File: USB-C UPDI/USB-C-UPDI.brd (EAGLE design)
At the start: 27.4 x 18.3 mm, 9 parts, among them IC1 FT232RL, J2 61300511121

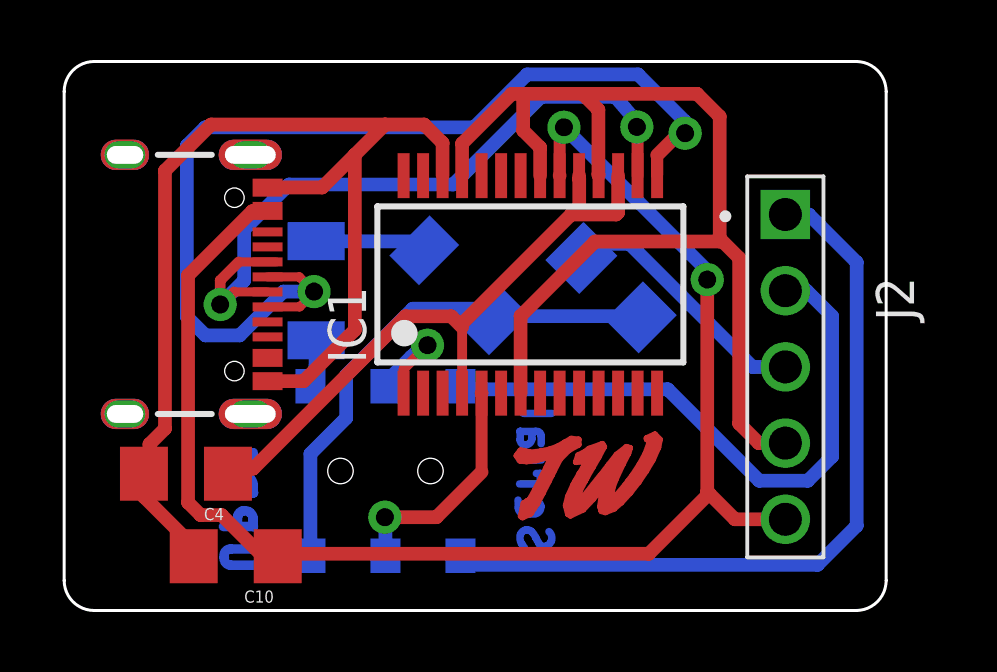
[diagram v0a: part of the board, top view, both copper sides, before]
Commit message: ftid2updi
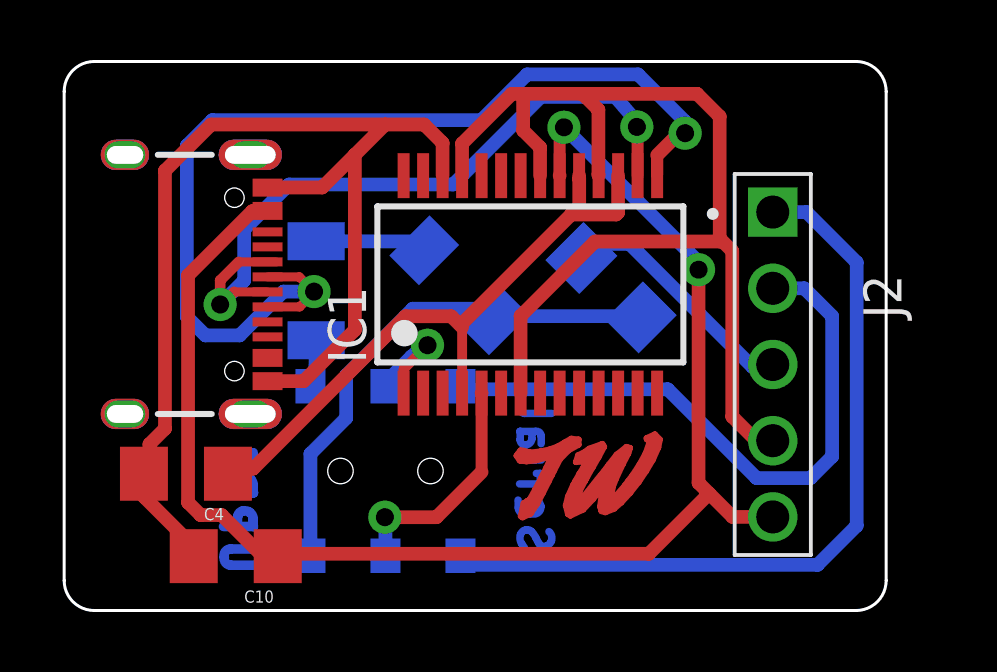
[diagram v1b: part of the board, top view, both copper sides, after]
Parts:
- moved J2 0.43 mm to (23.5, 11.8)

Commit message: updates
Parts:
- moved R1 2.52 mm to (10.8, 14.6), turned to 225 degrees
- moved D1 2.09 mm to (15.2, 14.4)
- moved R2 0.88 mm to (19.0, 14.6), turned to 225 degrees
- moved J2 0.71 mm to (24.2, 11.7)
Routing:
- net N$5: track 29.5 -> 0.00 mm, vias 1 -> 0
- net N$3: track 17.8 -> 3.35 mm
- net N$6: track 1.40 -> 11.5 mm, vias 0 -> 1
- net GND: track 78.1 -> 87.6 mm
- net VCC: track 48.4 -> 57.3 mm
- net N$10: track 4.02 -> 12.5 mm
- net N$7: track 7.77 -> 15.4 mm
- net N$11: track 1.58 -> 4.99 mm
- net UPDI: track 8.31 -> 5.05 mm
- net N$2: track 6.29 -> 8.72 mm
- net N$13: track 17.1 -> 16.3 mm
- net N$4: track 3.95 -> 4.61 mm

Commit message: updates
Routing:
- net GND: track 87.6 -> 84.3 mm
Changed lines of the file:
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@@
 <contactref element="J1" pad="VBUS2"/>
 <contactref element="J2" pad="5"/>
-<wire x1="16.4592" y1="20.1372" x2="16.3992" y2="20.1372" width="0.4572" layer="16"/>
+<wire x1="16.4592" y1="20.1272" x2="16.3992" y2="20.1272" width="0.4572" layer="16"/>
 <wire x1="21.746" y1="15.0004" x2="21.596" y2="15.0004" width="0.4572" layer="16"/>
-<via x="16.3992" y="20.1372" extent="1-16" drill="0.85" diameter="1.8"/>
+<via x="16.3992" y="20.1272" extent="1-16" drill="0.85" diameter="1.7"/>
 <via x="21.746" y="15.0004" extent="1-16" drill="0.85" diameter="1.8"/>
-<wire x1="16.3992" y1="20.1372" x2="16.417175" y2="20.119225" width="0.4572" layer="1"/>
-<wire x1="16.417175" y1="20.119225" x2="16.417175" y2="18.097175" width="0.4572" layer="1"/>
+<wire x1="16.3992" y1="20.1272" x2="16.417175" y2="20.109225" width="0.4572" layer="1"/>
+<wire x1="16.417175" y1="20.109225" x2="16.417175" y2="18.097175" width="0.4572" layer="1"/>
 <wire x1="16.417175" y1="18.097175" x2="16.415" y2="18.095" width="0.4572" layer="1"/>
 <wire x1="24.23" y1="6.66" x2="22.24" y2="6.66" width="0.4572" layer="1"/>
@@
 <wire x1="4.45" y1="6.78" x2="5.15" y2="6.78" width="0.4572" layer="1"/>
 <wire x1="17.031" y1="21.441" x2="20.42" y2="21.441" width="0.4572" layer="16"/>
-<wire x1="16.3992" y1="20.1372" x2="16.3992" y2="20.8092" width="0.4572" layer="16"/>
+<wire x1="16.3992" y1="20.1272" x2="16.3992" y2="20.8092" width="0.4572" layer="16"/>
 <wire x1="17.031" y1="21.441" x2="16.3992" y2="20.8092" width="0.4572" layer="16"/>
 <wire x1="20.42" y1="21.441" x2="22.74" y2="19.121" width="0.4572" layer="16"/>
 <wire x1="22.74" y1="16.07" x2="21.66" y2="14.99" width="0.4572" layer="16"/>
 <wire x1="22.74" y1="19.121" x2="22.74" y2="16.07" width="0.4572" layer="16"/>
-<wire x1="21.746" y1="15.0004" x2="21.66" y2="14.99" width="0" layer="19" extent="16-16"/>
+<wire x1="21.596" y1="15.0004" x2="21.66" y2="14.99" width="0" layer="19" extent="16-16"/>
 <wire x1="21.79" y1="7.07" x2="24.23" y2="6.66" width="0" layer="19" extent="1-1"/>
 <wire x1="6.68" y1="12.02" x2="6.68" y2="16.92" width="0" layer="19" extent="1-1"/>
@@
 <wire x1="12.515" y1="18.095" x2="12.515" y2="19.8" width="0.4572" layer="1"/>
 <wire x1="2.7432" y1="9.144" x2="3.23" y2="9.6308" width="0.4572" layer="1"/>
-<wire x1="4.8" y1="19.8" x2="9.14" y2="19.8" width="0.4572" layer="1"/>
+<wire x1="4.8" y1="19.8" x2="10.49" y2="19.8" width="0.4572" layer="1"/>
 <wire x1="10.49" y1="19.8" x2="12.515" y2="19.8" width="0.4572" layer="1"/>
-<wire x1="6.68" y1="17.695" x2="6.685" y2="17.7" width="0.4572" layer="1"/>
-<wire x1="7.04" y1="17.7" x2="9.14" y2="19.8" width="0.4572" layer="1"/>
+<wire x1="6.725" y1="17.7" x2="6.72" y2="17.695" width="0.4572" layer="1"/>
+<wire x1="6.68" y1="17.695" x2="6.72" y2="17.695" width="0.4572" layer="1"/>
 <wire x1="6.68" y1="11.245" x2="7.885" y2="11.245" width="0.4572" layer="1"/>
 <wire x1="7.885" y1="11.245" x2="10.49" y2="13.85" width="0.4572" layer="1"/>
@@
 <wire x1="13.155" y1="19.715" x2="14.86" y2="21.42" width="0.4572" layer="1"/>
 <wire x1="14.8816" y1="21.4416" x2="15.2" y2="21.4416" width="0.4572" layer="1"/>
-<wire x1="15.765" y1="18.095" x2="15.765" y2="18.935" width="0.4572" layer="1"/>
-<wire x1="15.765" y1="18.935" x2="14.86" y2="19.84" width="0.4572" layer="1"/>
-<wire x1="14.86" y1="19.84" x2="14.86" y2="21.42" width="0.4572" layer="1"/>
+<wire x1="15.765" y1="18.095" x2="15.765" y2="18.905" width="0.4572" layer="1"/>
+<wire x1="15.765" y1="18.905" x2="14.86" y2="19.81" width="0.4572" layer="1"/>
+<wire x1="14.86" y1="19.81" x2="14.86" y2="21.42" width="0.4572" layer="1"/>
 <wire x1="15.2" y1="21.4416" x2="15.2" y2="21.4516" width="0.4572" layer="1"/>
 <wire x1="2.56" y1="8.16" x2="2.56" y2="7.39" width="0.4572" layer="1"/>
@@
 <wire x1="15.115" y1="13.075" x2="16.66" y2="14.62" width="0.4572" layer="1"/>
 <wire x1="16.66" y1="14.62" x2="18.57" y2="14.62" width="0.4572" layer="1"/>
-<wire x1="6.685" y1="17.7" x2="7.04" y2="17.7" width="0.4572" layer="1"/>
-<wire x1="9.14" y1="19.8" x2="10.49" y2="19.8" width="0.4572" layer="1"/>
 <wire x1="10.49" y1="19.8" x2="10.49" y2="13.85" width="0.4572" layer="1"/>
 <wire x1="24.23" y1="9.2" x2="26.13" y2="11.1" width="0.4572" layer="1"/>
@@
 <wire x1="13.07" y1="19.8" x2="13.155" y2="19.715" width="0.4572" layer="1"/>
 <wire x1="15.765" y1="18.095" x2="17.715" y2="18.095" width="0" layer="19" extent="1-1"/>
+<wire x1="6.725" y1="17.7" x2="12.515" y2="18.095" width="0" layer="19" extent="1-1"/>
 </signal>
 <signal name="N$3">
@@
 <contactref element="S1" pad="1"/>
 <wire x1="20.0216" y1="10.9728" x2="13.4112" y2="10.9728" width="0.4572" layer="16"/>
-<wire x1="22.9796" y1="8.0148" x2="20.0216" y2="10.9728" width="0.4572" layer="16"/>
-<wire x1="24.7788" y1="8.0148" x2="22.9796" y2="8.0148" width="0.4572" layer="16"/>
-<wire x1="25.8584" y1="9.0944" x2="24.7788" y2="8.0148" width="0.4572" layer="16"/>
-<wire x1="25.8584" y1="13.0516" x2="25.8584" y2="9.0944" width="0.4572" layer="16"/>
+<wire x1="23.0696" y1="7.9248" x2="20.0216" y2="10.9728" width="0.4572" layer="16"/>
+<wire x1="25.0688" y1="7.9248" x2="23.0696" y2="7.9248" width="0.4572" layer="16"/>
+<wire x1="25.8584" y1="8.7144" x2="25.0688" y2="7.9248" width="0.4572" layer="16"/>
+<wire x1="25.8584" y1="13.0516" x2="25.8584" y2="8.7144" width="0.4572" layer="16"/>
 <wire x1="25.8584" y1="13.0516" x2="24.63" y2="14.28" width="0.4572" layer="16"/>
 <wire x1="24.23" y1="14.28" x2="24.63" y2="14.28" width="0.4572" layer="16"/>

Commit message: updates
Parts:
- added C1: 100nf, 01_SparkFun:1206
- added R3, R4: 5.1k, 01_SparkFun:1206
- added R5, R6: 330, 01_SparkFun:1206
- added RX-LED, TX-LED: LED, eagle_fab:LED1206
- C10: value 1uf -> 4.7uf
- moved J2 6.43 mm to (21.2, 6.04), turned to 0 degrees
- moved IC1 1.74 mm to (14.9, 12.8)
- moved D1 1.06 mm to (16.2, 14.4)
- moved R1 1.06 mm to (11.9, 14.6)
- moved R2 1.06 mm to (20.0, 14.6)
- moved S1 0.58 mm to (10.3, 7.75)
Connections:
- new net N$1: C1.1, IC1.17
- new net N$42: J1.B5, R3.1
- new net N$43: IC1.22, R6.1
- new net N$44: IC1.23, R5.1
- new net N$45: R5.2, RX-LED.2
- new net N$46: R6.2, TX-LED.2
- net GND: now also C1.2, J1.SHLD1, J1.SHLD2, J1.SHLD3, J1.SHLD4, R3.2, R4.2
- net N$9: now also J1.A5, R4.1; no longer C4.1, IC1.17, IC1.19, IC1.4
- net VCC: now also C4.1, IC1.4, RX-LED.1, TX-LED.1
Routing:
- net RX: track 26.1 -> 3.82 mm
- net GND: track 84.3 -> 103.4 mm
- net N$13: track 16.3 -> 0.00 mm, vias 1 -> 0
- net N$7: track 15.4 -> 0.00 mm, vias 1 -> 0
- net N$3: track 3.35 -> 17.6 mm
- net N$10: track 12.5 -> 0.00 mm, vias 1 -> 0
- net TX: track 20.8 -> 8.58 mm
- net N$9: track 21.7 -> 9.96 mm
- net N$6: track 11.5 -> 0.00 mm
- net N$42: track 0.00 -> 11.1 mm
- net N$44: track 0.00 -> 6.48 mm
- net VCC: track 57.3 -> 51.0 mm, vias 2 -> 0
- net N$43: track 0.00 -> 5.57 mm
- net N$1: track 0.00 -> 5.53 mm
- net N$45: track 0.00 -> 4.15 mm
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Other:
- board size 27.4 x 18.3 mm -> 5 x 8.6 mm

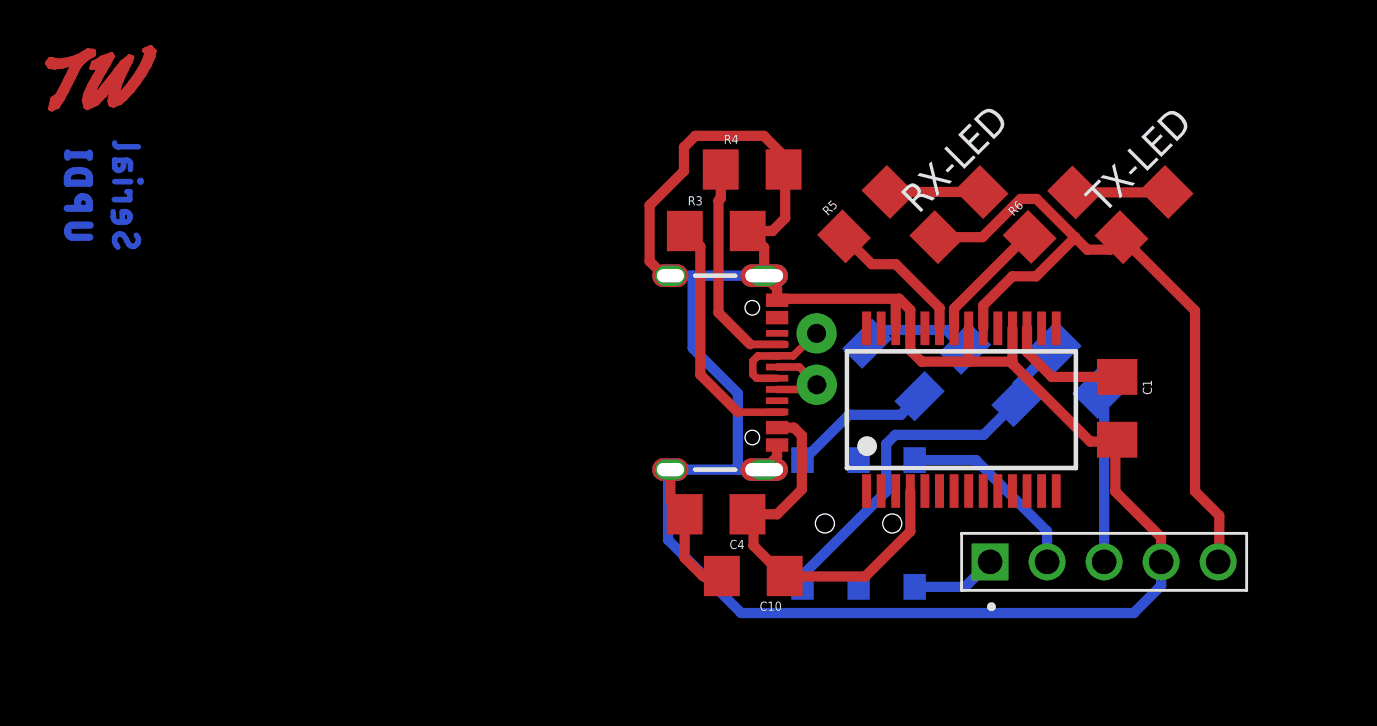
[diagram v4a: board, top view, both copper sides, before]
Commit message: UPDI updates
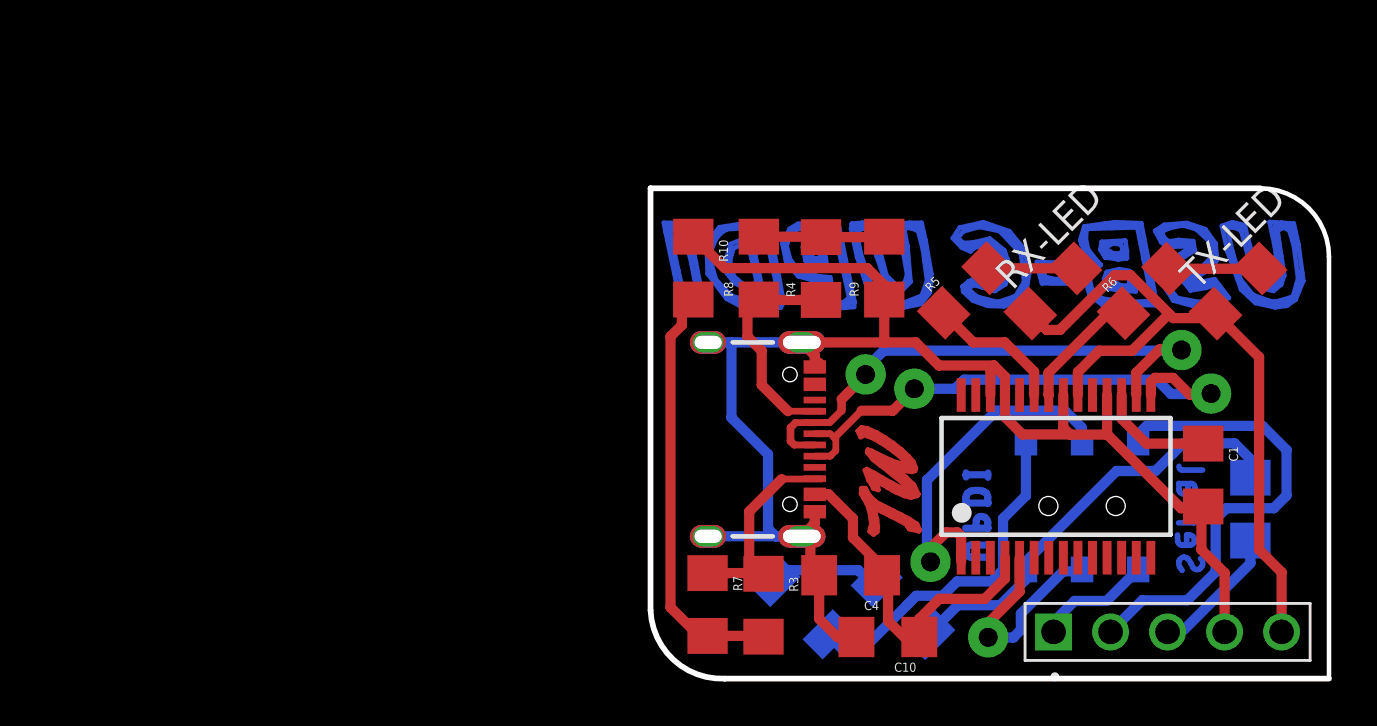
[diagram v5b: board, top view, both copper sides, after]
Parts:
- added R10, R9: 100, 01_SparkFun:1206
- added R7, R8: 10k, 01_SparkFun:1206
- C10: value 4.7uf -> 1uf
- R3, R4: value 5.1k -> 10k
- moved R3 16.8 mm to (6.07, 4.11), turned to 270 degrees
- moved R1 11.4 mm to (7.77, 3.98)
- moved D1 11.1 mm to (12.3, 4.00)
- moved S1 9.99 mm to (20.3, 8.53)
- moved R2 9.91 mm to (27.8, 8.39), turned to 270 degrees
- moved C10 6.58 mm to (11.6, 2.69)
- moved C4 6.58 mm to (9.95, 5.44)
- moved R5 5.59 mm to (15.1, 18.1)
- moved RX-LED 5.39 mm to (19.0, 18.1)
- moved R6 5.39 mm to (23.1, 18.1)
- moved TX-LED 5.39 mm to (27.2, 18.1)
- moved R4 5.37 mm to (8.64, 19.1), turned to 90 degrees
- moved IC1 5.16 mm to (19.1, 9.85)
- moved C1 4.85 mm to (25.7, 9.91)
- moved J2 4.21 mm to (24.1, 2.92)
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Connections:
- new net N$49: J1.B5, R3.1, R7.1
- new net N$50: R10.2, R3.2, R7.2
- net GND: now also R10.1, R9.1; no longer R3.2, R4.2
- net N$42: now also R4.2, R8.2, R9.2; no longer J1.B5, R3.1
- net N$9: now also R8.1
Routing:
- net GND: track 103.4 -> 73.7 mm
- net N$50: track 0.00 -> 18.8 mm
- net N$63: track 0.00 -> 17.6 mm
- net N$51: track 0.00 -> 17.4 mm
- net N$10: track 0.00 -> 16.1 mm
- net N$53: track 0.00 -> 15.6 mm
- net N$52: track 0.00 -> 15.6 mm
- net N$64: track 0.00 -> 15.5 mm
- net N$61: track 0.00 -> 15.2 mm
- net N$6: track 0.00 -> 14.4 mm
- net N$54: track 0.00 -> 14.0 mm
- net N$8: track 0.00 -> 13.6 mm
- net N$62: track 0.00 -> 13.5 mm
- net TX: track 8.58 -> 21.3 mm
- net N$55: track 0.00 -> 12.7 mm
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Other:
- board size 5 x 8.6 mm -> 30.2 x 21.8 mm
